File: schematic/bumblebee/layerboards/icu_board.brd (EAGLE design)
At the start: 85 x 100 mm, 22 parts

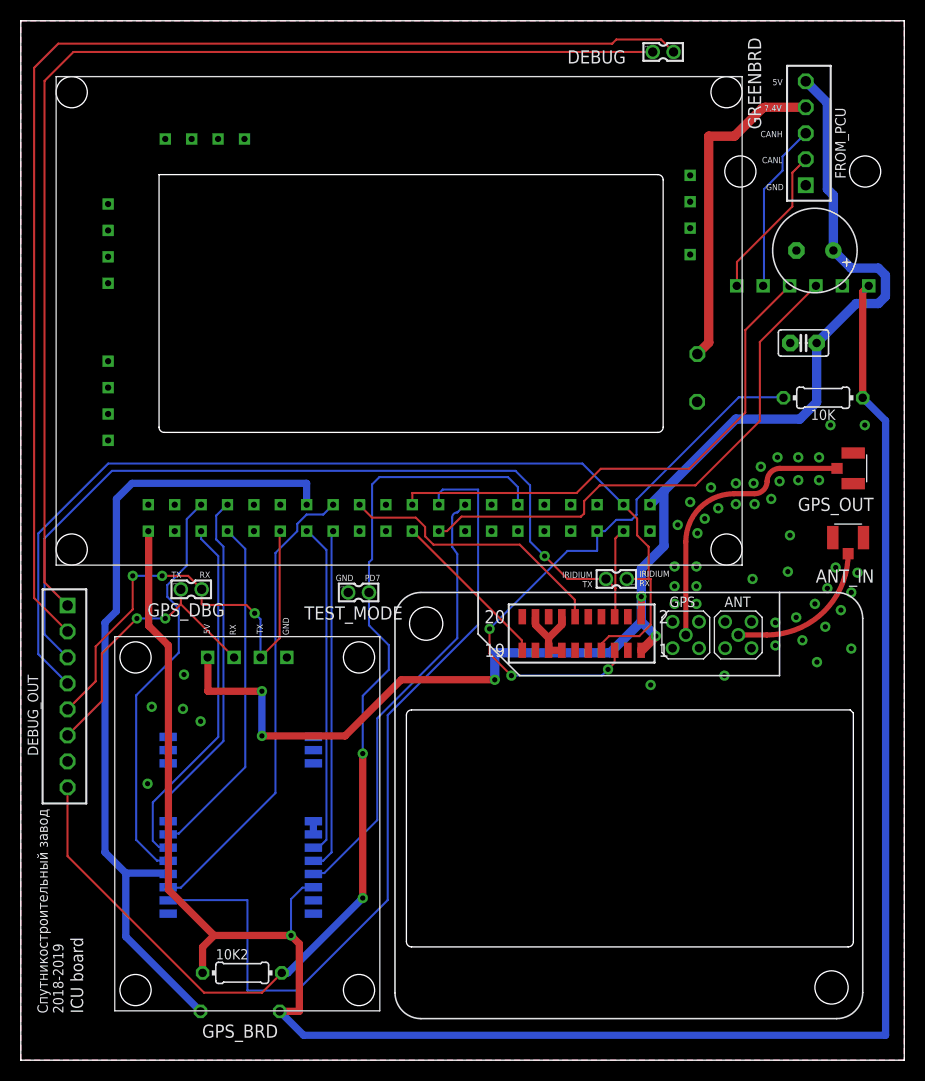
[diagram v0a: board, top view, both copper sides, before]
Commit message: Исправил библиотеку Осталось исправить внешнюю плату и сделать плату под антенну GPS
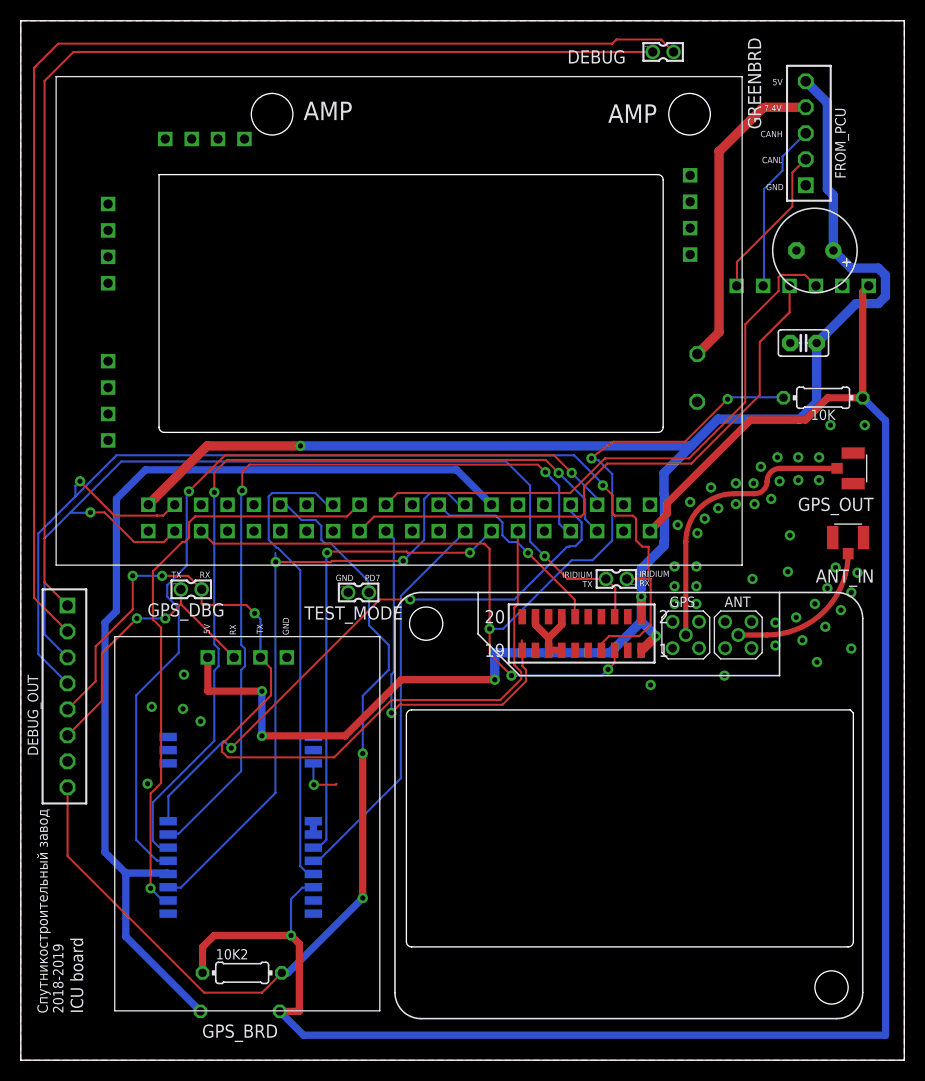
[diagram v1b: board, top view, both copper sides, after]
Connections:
- net N$10: now also CAN.CTX; no longer CAN.CRX
- net N$9: now also CAN.CRX; no longer CAN.CTX
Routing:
- net 5V_ICU: track 134.6 -> 188.3 mm, vias 5 -> 6
- net N$15: track 34.8 -> 81.3 mm, vias 0 -> 2
- net TX_GPS: track 46.9 -> 92.3 mm
- net N$16: track 39.7 -> 83.5 mm, vias 0 -> 2
- net ON_OFF: track 56.5 -> 98.5 mm, vias 3 -> 5
- net N$8: track 33.5 -> 75.4 mm, vias 0 -> 2
- net N$12: track 81.6 -> 56.9 mm, vias 0 -> 1
- net N$2: track 33.4 -> 56.8 mm, vias 0 -> 2
- net NETWORK_AVAILABLE: track 15.9 -> 36.2 mm, vias 0 -> 1
- net N$18: track 78.7 -> 96.3 mm
- net N$17: track 45.1 -> 61.0 mm, vias 0 -> 2
- net 3.3V: track 201.1 -> 186.0 mm
- net DF_S_RX: track 97.3 -> 111.9 mm, vias 0 -> 2
- net N$6: track 32.1 -> 46.3 mm, vias 0 -> 2
- net PD7: track 102.4 -> 88.9 mm
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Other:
- board text added: "AMP"
